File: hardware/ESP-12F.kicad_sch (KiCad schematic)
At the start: 38 parts, among them J10 PROG_PORT, U10 ESP-12F, U11 MCP2558FD-xMF, U6 AT24CS01-STUM, U8 PI4IOE5V6416LEX, U9 PI4IOE5V6416LEX

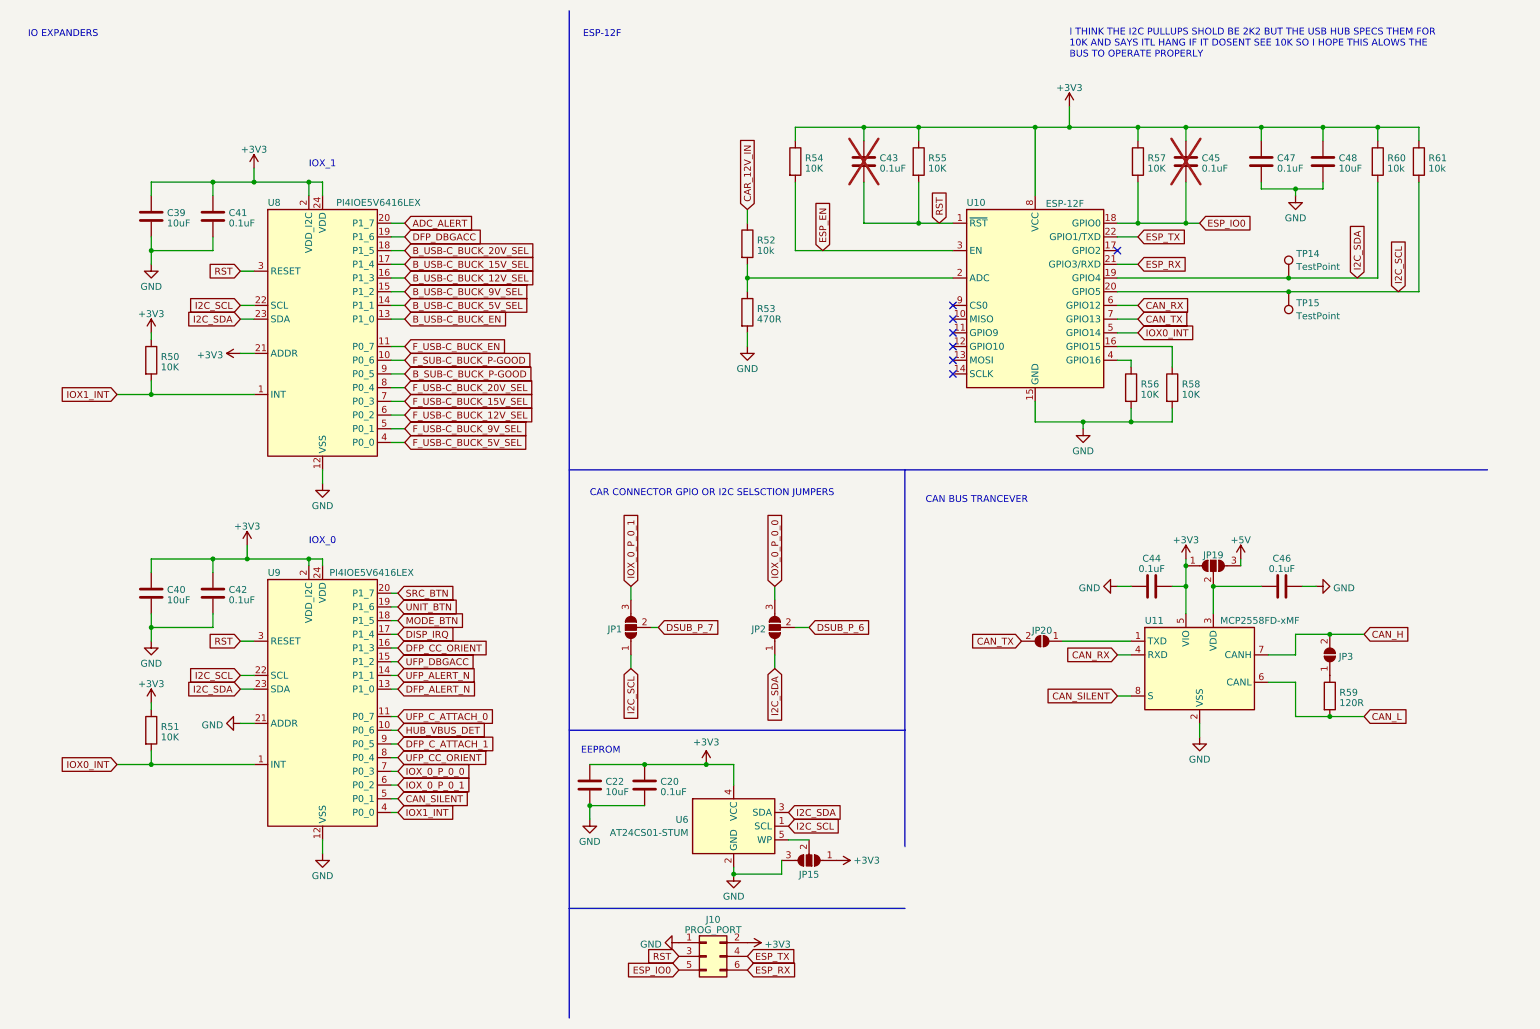
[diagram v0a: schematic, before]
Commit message: switched can tranceiver to combo controler and tranceiver
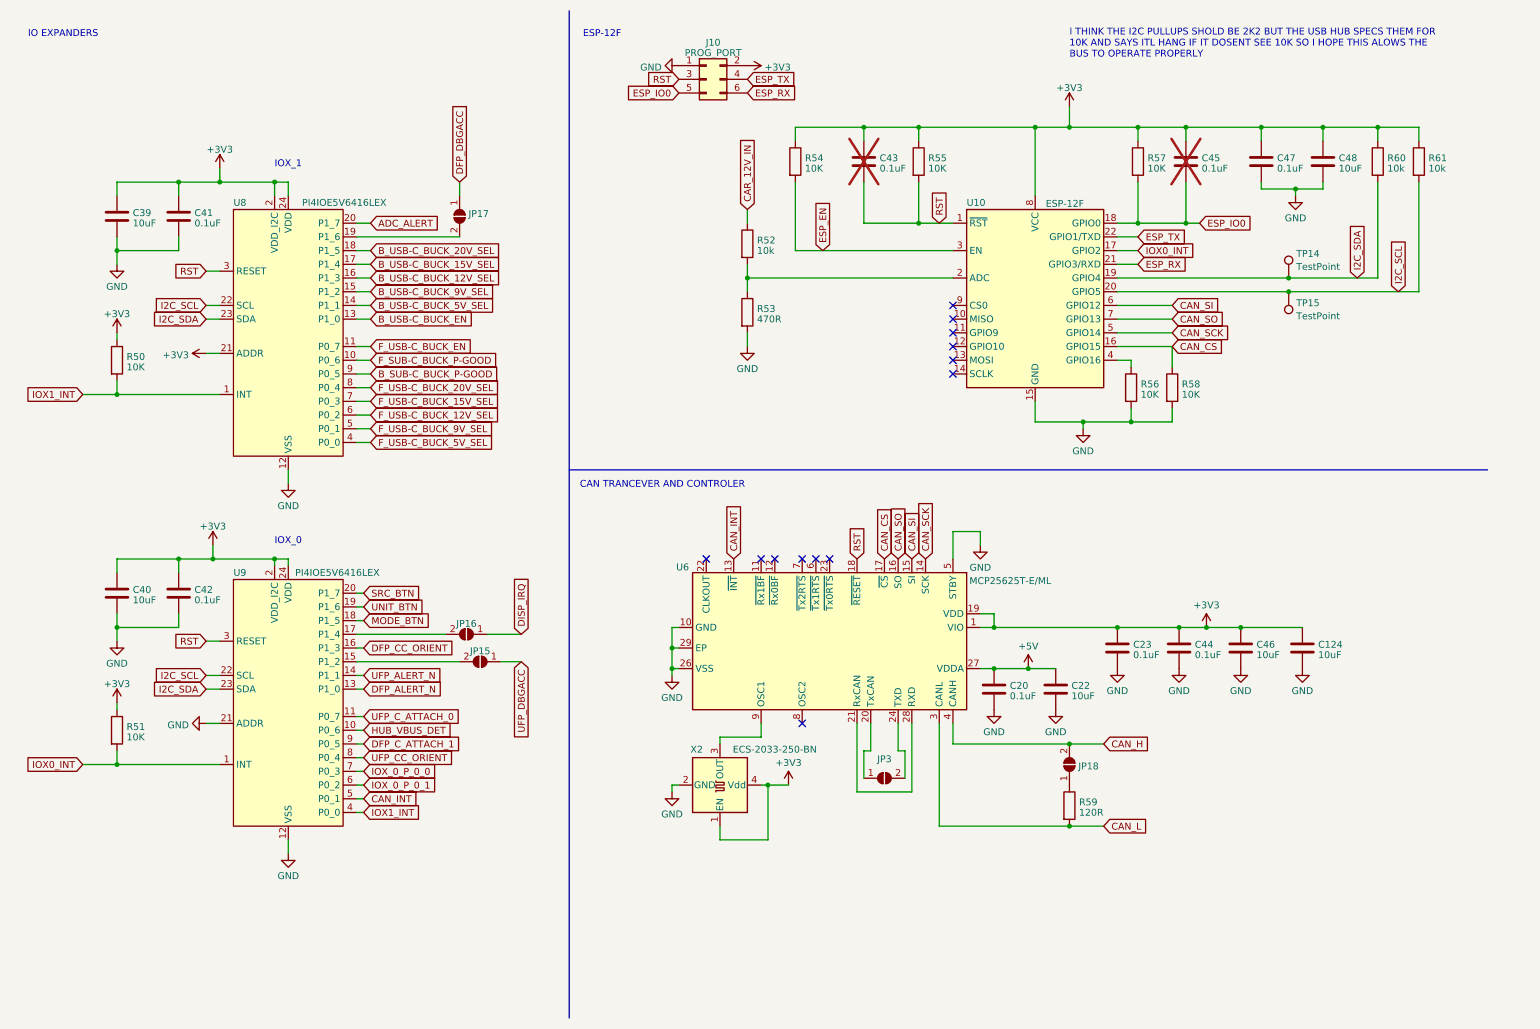
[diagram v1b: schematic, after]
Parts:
- removed JP1, JP15, JP19, JP2: ~, Jumper:SolderJumper-3_P1.3mm_Open_RoundedPad1.0x1.5mm_NumberLabels, symbol Jumper:SolderJumper_3_Open
- removed JP20: ~, Jumper:SolderJumper-2_P1.3mm_Open_RoundedPad1.0x1.5mm, symbol Jumper:SolderJumper_2_Open
- removed U11: MCP2558FD-xMF, Package_DFN_QFN:DFN-8-1EP_3x3mm_P0.65mm_EP1.55x2.4mm, symbol Interface_CAN_LIN:MCP2557FD-xMF
- removed U6: AT24CS01-STUM, Package_TO_SOT_SMD:SOT-23-5, symbol Memory_EEPROM:AT24CS01-STUM
- added C124: 10uF, Capacitor_SMD:C_0603_1608Metric, symbol Device:C
- added C23: 0.1uF, Capacitor_SMD:C_0603_1608Metric, symbol Device:C
- added JP15, JP16, JP17, JP18: ~, Jumper:SolderJumper-2_P1.3mm_Open_RoundedPad1.0x1.5mm, symbol Jumper:SolderJumper_2_Open
- added U6: MCP25625T-E/ML, CARTHING:28-QFN-EP, symbol Interface_CAN_LIN:MCP25625-x-SS
- added X2: ECS-2033-250-BN, Oscillator:Oscillator_SMD_Kyocera_KC2520Z-4Pin_2.5x2.0mm, symbol Oscillator:TXC-7C
- C46: value 0.1uF -> 10uF
- TP14, TP15: footprint TestPoint:TestPoint_Pad_D1.5mm -> TestPoint:TestPoint_Pad_D1.0mm
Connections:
- net +3V3: now also C44.1, C46.1, C124.1, C23.1, U6.1 (VIO), U6.19 (VDD), X2.1 (EN), X2.4 (Vdd); no longer C20.1, C22.1, C44.2
- net +5V: now also C20.1, C22.1, U6.27 (VDDA)
- net CAN_H: now also JP18.2 (B), U6.4 (CANH); no longer JP3.2 (B)
- net CAN_L: now also U6.3 (CANL)
- net DFP_DBGACC: now also JP17.1 (A); no longer U8.19 (P1_6)
- net DISP_IRQ: now also JP16.1 (A); no longer U9.17 (P1_4)
- net GND: now also C44.2, C124.2, C23.2, U6.10 (GND), U6.26 (VSS), U6.29 (EP), U6.5 (STBY), X2.2 (GND); no longer C44.1
- net IOX0_INT: now also U10.17 (GPIO2); no longer U10.5 (GPIO14)
- net RST: now also U6.18 (~{RESET})
- net UFP_DBGACC: now also JP15.1 (A); no longer U9.15 (P1_2)
- net at R59.1: now also JP18.1 (A); no longer JP3.1 (A)
- net CAN_CS: now reaches R58.1, U10.16 (GPIO15)
- net CAN_CS: now also U6.17 (~{CS})
- net CAN_RX renamed CAN_SI
- net CAN_SI: now also U6.15 (SI)
- net CAN_SILENT renamed CAN_INT
- net CAN_INT: now also U6.13 (~{INT})
- net CAN_TX renamed CAN_SO
- net CAN_SO: now also U6.16 (SO)
- new net: JP17.2 (B), U8.19 (P1_6)
- new net: JP15.2 (B), U9.15 (P1_2)
- new net: JP3.1 (A), U6.20 (TxCAN)
- new net: U6.21 (RxCAN), U6.28 (RXD)
- new net: JP3.2 (B), U6.24 (TXD)
- new net: U6.9 (OSC1), X2.3 (OUT)
- new net: JP16.2 (B), U9.17 (P1_4)
- new net CAN_SCK: U10.5 (GPIO14), U6.14 (SCK)
- no-connect marks 7 -> 13
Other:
- note added: "CAN TRANCEVER AND CONTROLER"
- note removed: "CAN BUS TRANCEVER"
- note removed: "CAR CONNECTOR GPIO OR I2C SELSCTION JUMPERS"
- note removed: "EEPROM"
- moved on the sheet: C39, C40, C41, C42, J10, R50, R51, U8, U9

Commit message: kicad version upgrade and minor pcb changes
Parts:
- added TP38, TP39, TP40, TP41, TP42, TP43, TP44, TP45: TestPoint, TestPoint:TestPoint_Pad_D1.0mm, symbol Connector:TestPoint
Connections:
- net at U6.11 (~{Rx1BF}): now also TP38.1
- net at U6.12 (~{Rx0BF}): now also TP39.1
- net at U6.21 (RxCAN), U6.28 (RXD): now also TP44.1
- net at U6.22 (CLKOUT): now also TP40.1
- net at U6.23 (~{Tx0RTS}): now also TP43.1
- net at U6.6 (~{Tx1RTS}): now also TP42.1
- net at U6.7 (~{Tx2RTS}): now also TP41.1
- net at U6.9 (OSC1), X2.3 (OUT): now also TP45.1
- no-connect marks 13 -> 7

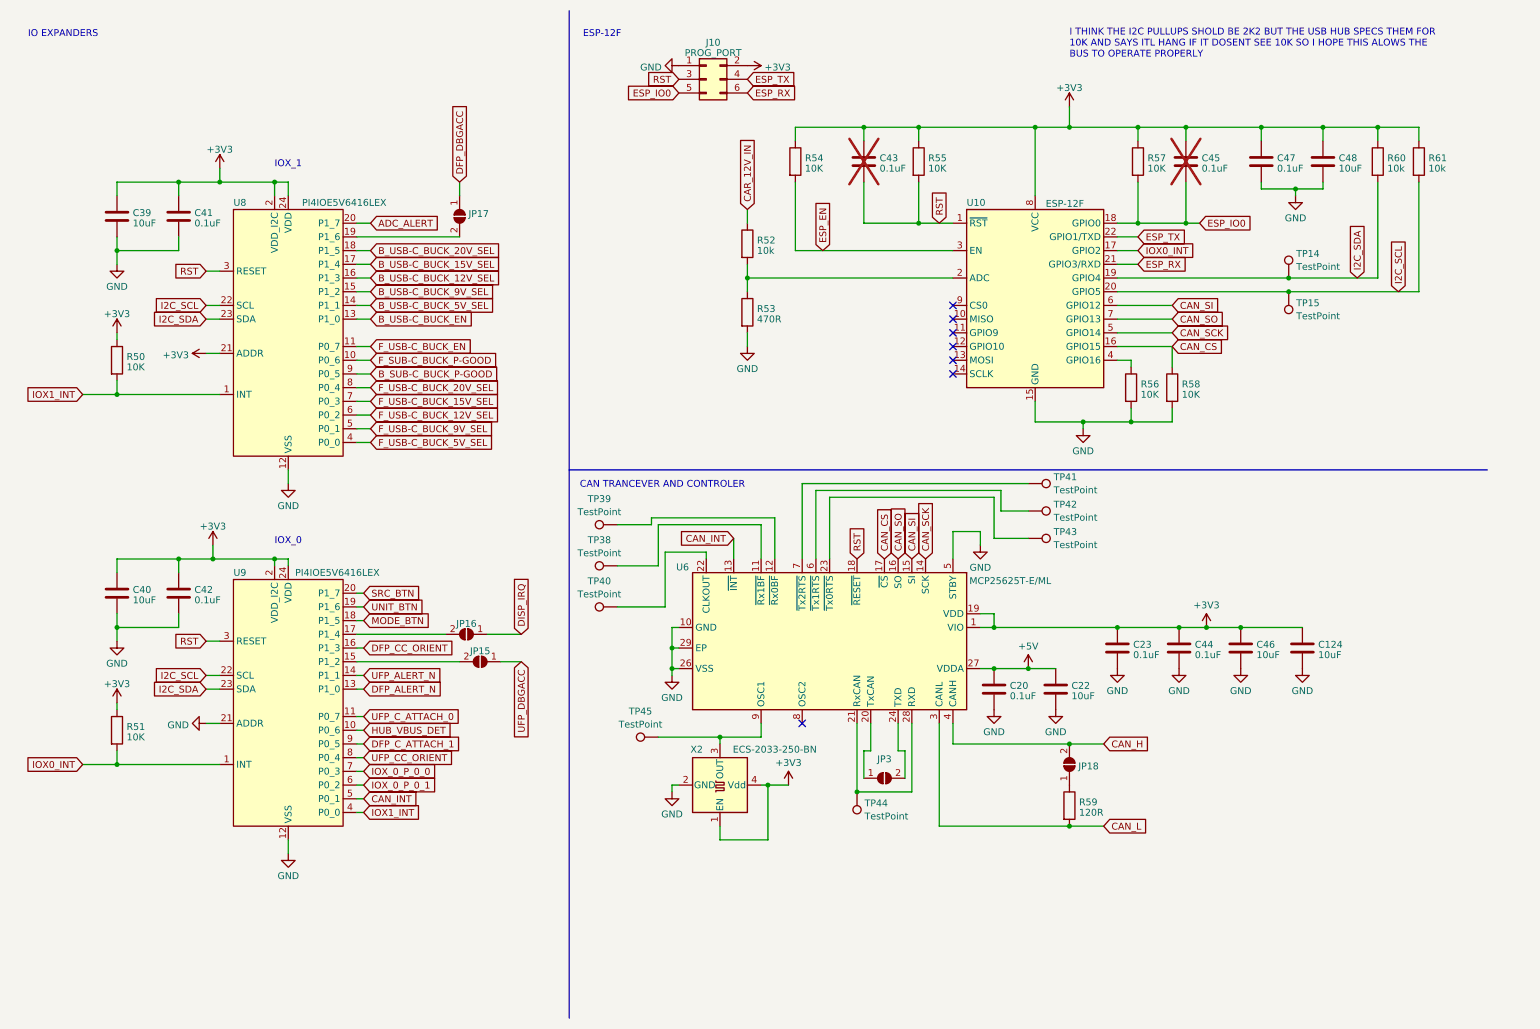
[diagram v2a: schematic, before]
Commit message: migrated to the esp32-s2 and starting new board revison
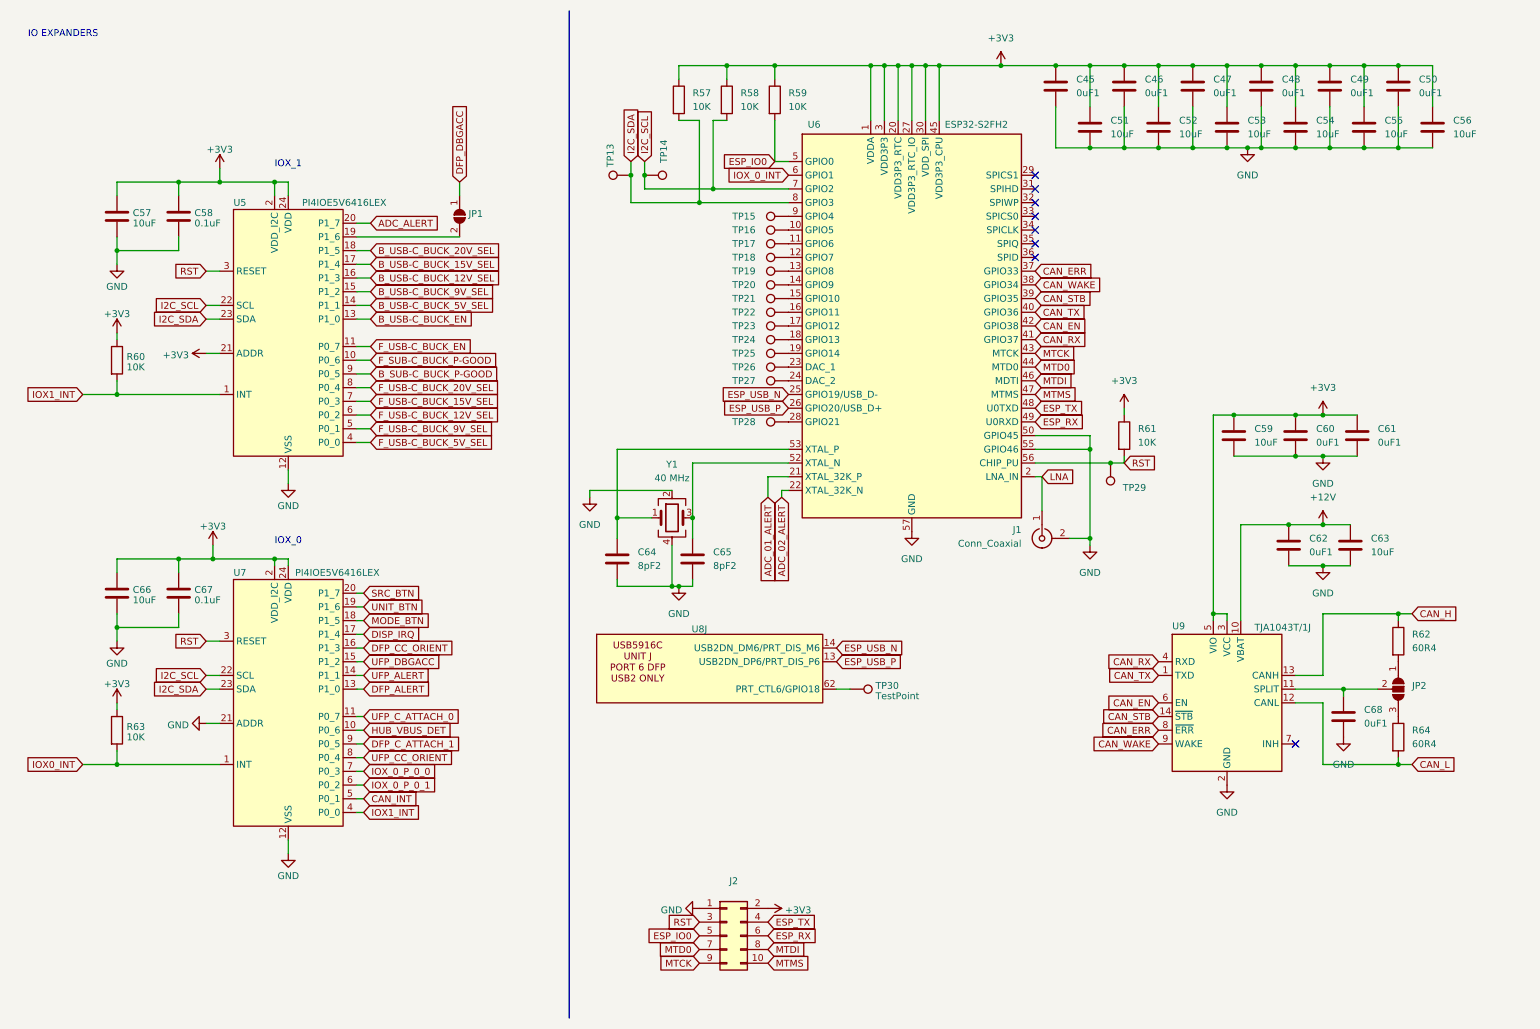
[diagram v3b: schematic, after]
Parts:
- removed C124, C22: 10uF, Capacitor_SMD:C_0603_1608Metric, symbol Device:C
- removed C20, C23, C43, C44: 0.1uF, Capacitor_SMD:C_0603_1608Metric, symbol Device:C
- removed J10: PROG_PORT, Connector_PinHeader_2.54mm:PinHeader_2x03_P2.54mm_Vertical, symbol Connector_Generic:Conn_02x03_Odd_Even
- removed JP15, JP16, JP18, JP3: ~, Jumper:SolderJumper-2_P1.3mm_Open_RoundedPad1.0x1.5mm, symbol Jumper:SolderJumper_2_Open
- removed R52, R60: 10k, Resistor_SMD:R_0603_1608Metric, symbol Device:R
- removed R53: 470R, Resistor_SMD:R_0603_1608Metric, symbol Device:R
- removed R54, R55, R56: 10K, Resistor_SMD:R_0603_1608Metric, symbol Device:R
- removed TP38, TP39, TP40, TP41, TP42, TP43, TP44, TP45: TestPoint, TestPoint:TestPoint_Pad_D1.0mm, symbol Connector:TestPoint
- removed U10: ESP-12F, RF_Module:ESP-12E, symbol RF_Module:ESP-12F
- removed U6: MCP25625T-E/ML, CARTHING:28-QFN-EP, symbol Interface_CAN_LIN:MCP25625-x-SS
- removed X2: ECS-2033-250-BN, Oscillator:Oscillator_SMD_Kyocera_KC2520Z-4Pin_2.5x2.0mm, symbol Oscillator:TXC-7C
- added C49, C50, C60, C61, C62, C68: 0uF1, Capacitor_SMD:C_0603_1608Metric, symbol Device:C
- added C51, C52, C53, C54, C55, C56, C59, C63: 10uF, Capacitor_SMD:C_0603_1608Metric, symbol Device:C
- added C64, C65: 8pF2, Capacitor_SMD:C_0603_1608Metric, symbol Device:C
- added J1: Conn_Coaxial, Connector_Coaxial:SMA_Amphenol_132291-12_Vertical, symbol Connector:Conn_Coaxial
- added J2: ~, Connector_PinHeader_2.54mm:PinHeader_2x05_P2.54mm_Vertical, symbol Connector_Generic:Conn_02x05_Odd_Even
- added JP2: ~, Jumper:SolderJumper-3_P2.0mm_Open_TrianglePad1.0x1.5mm, symbol Jumper:SolderJumper_3_Open
- added R62, R64: 60R4, Resistor_SMD:R_0603_1608Metric, symbol Device:R
- added TP13, TP16, TP17, TP18, TP19, TP20, TP21, TP22, TP23, TP24, TP25, TP26, TP27, TP28, TP29: ~, TestPoint:TestPoint_Pad_D1.0mm, symbol Connector:TestPoint
- added TP30: TestPoint, TestPoint:TestPoint_Pad_D1.0mm, symbol Connector:TestPoint
- added U6: ESP32-S2FH2, Package_DFN_QFN:QFN-56-1EP_7x7mm_P0.4mm_EP4x4mm, symbol MCU_Espressif:ESP32-S2
- added U8: USB5926C, CARTHING:VQFN100_KD_MCH, symbol CARTHING:USB5916C
- added U9: TJA1043T/1J, Package_SO:SOIC-14_3.9x8.7mm_P1.27mm, symbol Interface_CAN_LIN:TJA1043T
- added Y1: 40 MHz, CARTHING:cx3225sa_e, symbol Device:Crystal_GND23
- C45: value 0.1uF -> 0uF1; Digikey Part Number (none) -> 399-C0603C104M5RACTUCT-ND; now fitted
- C46, C48: value 10uF -> 0uF1; Digikey Part Number (none) -> 399-C0603C104M5RACTUCT-ND
- C47: value 0.1uF -> 0uF1; Digikey Part Number (none) -> 399-C0603C104M5RACTUCT-ND
- R57, R58: Digikey Part Number (none) -> 541-1.00KHCT-ND
- R59: value 120R -> 10K; Digikey Part Number (none) -> RMCF0603JT10K0CT-ND
- R61: value 10k -> 10K; Digikey Part Number (none) -> RMCF0603JT10K0CT-ND
- TP14, TP15: value TestPoint -> ~; now left out of the parts list
- U5: renamed from U8; footprint PCM_Package_SO_AKL:TSSOP-24_4.4x7.8mm_P0.65mm -> Package_SO:TSSOP-24_4.4x7.8mm_P0.65mm
- U7: renamed from U9; footprint PCM_Package_SO_AKL:TSSOP-24_4.4x7.8mm_P0.65mm -> Package_SO:TSSOP-24_4.4x7.8mm_P0.65mm
- renumbered C39 to C57, C41 to C58, C40 to C66, C42 to C67, JP17 to JP1, R50 to R60, R51 to R63
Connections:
- net CAN_CS is gone; now on net +3V3: R58.1
- net +3V3: now also R59.1, C49.1, C50.1, C51.1, C52.1, C53.1, C54.1, C55.1, C56.1, C59.1, C60.1, C61.1, J2.2 (Pin_2), U6.1 (VDDA), U6.20 (VDD3P3_RTC), U6.27 (VDD3P3_RTC_IO), U6.3 (VDD3P3), U6.30 (VDD_SPI), U6.4 (VDD3P3), U6.45 (VDD3P3_CPU), U6.51 (VDDA), U6.54 (VDDA), U9.3 (VCC), U9.5 (VIO)
- net CAN_H: now also R62.1, U9.13 (CANH)
- net CAN_L: now also R64.2, U9.12 (CANL); no longer R59.2
- net DISP_IRQ: now also U7.17 (P1_4)
- net ESP_IO0: now also R59.2, J2.5 (Pin_5), U6.5 (GPIO0); no longer C45.2, R57.2
- net ESP_RX: now also J2.6 (Pin_6), U6.49 (U0RXD)
- net ESP_TX: now also J2.4 (Pin_4), U6.48 (U0TXD)
- net GND: now also C45.2, C49.2, C50.2, C51.2, C52.2, C53.2, C54.2, C55.2, C56.2, C59.2, C60.2, C61.2, C62.2, C63.2, C64.2, C65.2, C68.2, J1.2 (Ext), J2.1 (Pin_1), U6.50 (GPIO45), U6.55 (GPIO46), U6.57 (GND), U9.2 (GND), Y1.2, Y1.4; no longer R58.2
- net I2C_SCL: now also R58.2, TP14.1, U6.7 (GPIO2); no longer R61.2, TP15.1
- net I2C_SDA: now also R57.2, TP13.1, U6.8 (GPIO3); no longer TP14.1
- net RST: now also R61.2, J2.3 (Pin_3), TP29.1, U6.56 (CHIP_PU)
- net UFP_DBGACC: now also U7.15 (P1_2)
- net DFP_ALERT_N renamed DFP_ALERT
- net UFP_ALERT_N renamed UFP_ALERT
- new net: TP15.1, U6.9 (GPIO4)
- new net: TP20.1, U6.14 (GPIO9)
- new net: JP2.1 (A), R62.2
- new net: C64.1, U6.53 (XTAL_P), Y1.1
- new net: TP19.1, U6.13 (GPIO8)
- new net: TP24.1, U6.18 (GPIO13)
- new net: TP27.1, U6.24 (DAC_2)
- new net: TP16.1, U6.10 (GPIO5)
- new net: C65.1, U6.52 (XTAL_N), Y1.3
- new net: TP18.1, U6.12 (GPIO7)
- new net: TP25.1, U6.19 (GPIO14)
- new net: C68.1, JP2.2 (C), U9.11 (SPLIT)
- new net: JP2.3 (B), R64.1
- new net: TP22.1, U6.16 (GPIO11)
- new net: TP17.1, U6.11 (GPIO6)
- new net: TP23.1, U6.17 (GPIO12)
- new net: TP30.1, U8.62 (PRT_CTL6/GPIO18)
- new net: TP26.1, U6.23 (DAC_1)
- new net: TP21.1, U6.15 (GPIO10)
- new net: TP28.1, U6.28 (GPIO21)
- new net +12V: C62.1, C63.1, U9.10 (VBAT)
- new net ADC_01_ALERT: U6.21 (XTAL_32K_P)
- new net ADC_02_ALERT: U6.22 (XTAL_32K_N)
- new net CAN_EN: U6.42 (GPIO38), U9.6 (EN)
- new net CAN_ERR: U6.37 (GPIO33), U9.8 (~{ERR})
- new net CAN_RX: U6.41 (GPIO37), U9.4 (RXD)
- new net CAN_STB: U6.39 (GPIO35), U9.14 (~{STB})
- new net CAN_TX: U6.40 (GPIO36), U9.1 (TXD)
- new net CAN_WAKE: U6.38 (GPIO34), U9.9 (WAKE)
- new net ESP_USB_N: U6.25 (GPIO19/USB_D-), U8.14 (USB2DN_DM6/PRT_DIS_M6)
- new net ESP_USB_P: U6.26 (GPIO20/USB_D+), U8.13 (USB2DN_DP6/PRT_DIS_P6)
- new net IOX_0_INT: U6.6 (GPIO1)
- new net LNA: J1.1 (In), U6.2 (LNA_IN)
- new net MTCK: J2.9 (Pin_9), U6.43 (MTCK)
- new net MTD0: J2.7 (Pin_7), U6.44 (MTD0)
- new net MTDI: J2.8 (Pin_8), U6.46 (MDTI)
- new net MTMS: J2.10 (Pin_10), U6.47 (MTMS)
- no-connect marks 7 -> 8
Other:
- note removed: "CAN TRANCEVER AND CONTROLER"
- note removed: "ESP-12F"
- note removed: "I THINK THE I2C PULLUPS SHOLD BE 2K2 BUT THE USB HUB SPECS THEM FOR 10K AND SAYS ITL HANG IF IT DOSENT SEE 10K SO I HOPE THIS ALOWS THE BUS TO OPERATE PROPERLY"
